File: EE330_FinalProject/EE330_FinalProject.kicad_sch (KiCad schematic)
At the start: 20 parts, among them IC1 LT1490AIS8#PBF, J1 01x04_Pin, Q1 2N3904, Q2 2N3904, Q3 2N3904, Q4 2N3904

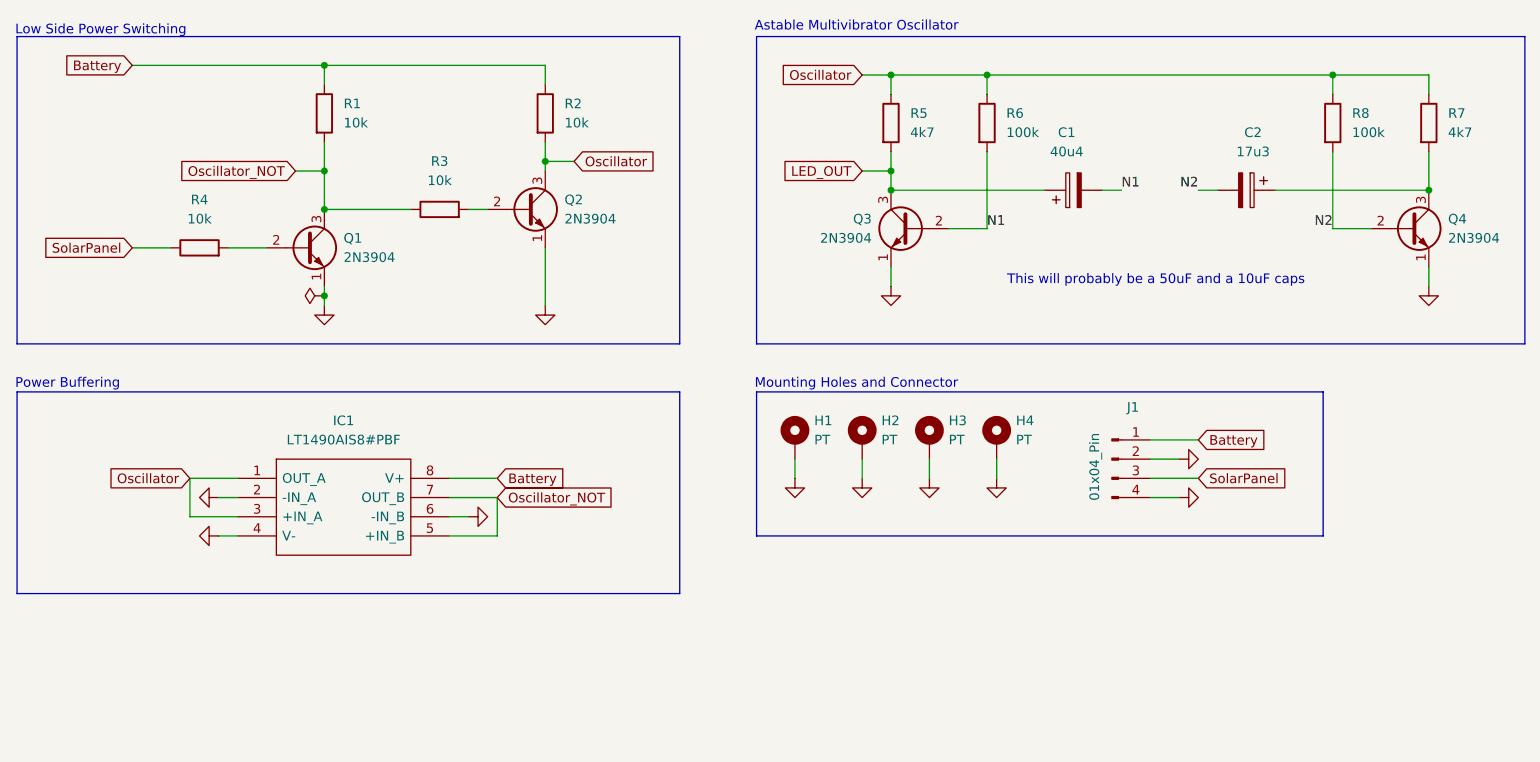
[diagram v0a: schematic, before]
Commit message: Updated schematic and PCB based on the testing done today. Need to confirm physical setup before finalizing
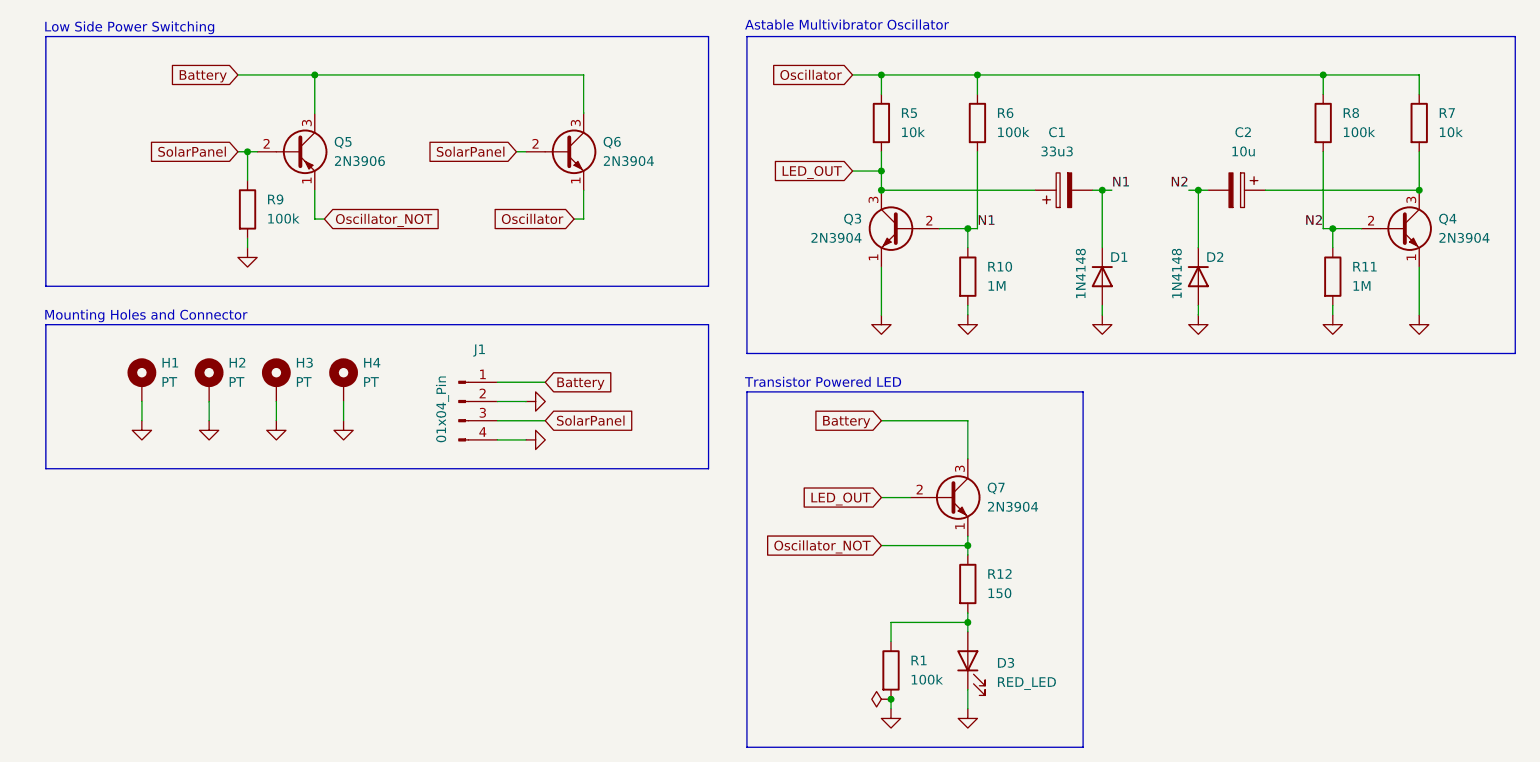
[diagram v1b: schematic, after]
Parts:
- removed IC1: LT1490AIS8#PBF, Circuit_Craft_Footprints:LT1490, symbol Circuit_Craft_Symbols:LT1490AIS8#PBF
- removed Q1, Q2: 2N3904, Package_TO_SOT_THT:TO-92_Inline, symbol Transistor_BJT:2N3904
- removed R2, R3, R4: 10k, Resistor_SMD:R_0603_1608Metric, symbol Device:R
- added D1, D2: 1N4148, Diode_THT:D_DO-35_SOD27_P7.62mm_Horizontal, symbol Diode:1N4148
- added D3: RED_LED, LED_SMD:LED_0805_2012Metric, symbol Device:LED
- added Q5: 2N3906, Package_TO_SOT_THT:TO-92_Inline, symbol Transistor_BJT:2N3906
- added Q6, Q7: 2N3904, Package_TO_SOT_THT:TO-92_Inline, symbol Transistor_BJT:2N3904
- added R10, R11: 1M, Resistor_SMD:R_0603_1608Metric, symbol Device:R
- added R12: 150, Resistor_SMD:R_0603_1608Metric, symbol Device:R
- added R9: 100k, Resistor_SMD:R_0603_1608Metric, symbol Device:R
- C1: value 40u4 -> 33u3
- C2: value 17u3 -> 10u
- R1: value 10k -> 100k
- R5, R7: value 4k7 -> 10k
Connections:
- net Battery: now also Q5.3 (C), Q6.3 (C), Q7.3 (C); no longer R1.1
- net GND: now also R1.2, D1.2 (A), D2.2 (A), D3.1 (K), R10.2, R11.2, R9.2
- net LED_OUT: now also Q7.2 (B)
- net N1: now also D1.1 (K), R10.1
- net N2: now also D2.1 (K), R11.1
- net Oscillator: now also Q6.1 (E)
- net Oscillator_NOT: now also Q5.1 (E), Q7.1 (E), R12.1; no longer R1.2
- net SolarPanel: now also Q5.2 (B), Q6.2 (B), R9.1
- new net: D3.2 (A), R1.1, R12.2
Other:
- note added: "Transistor Powered LED"
- note removed: "Power Buffering"
- note removed: "This will probably be a 50uF and a 10uF caps"
- moved on the sheet: C1, C2, H1, H2, H3, H4, J1, Q3, Q4, R5, R6, R7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
